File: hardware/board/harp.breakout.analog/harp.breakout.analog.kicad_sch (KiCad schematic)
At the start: 19 parts, among them J1 Conn_01x12_Socket, J10 Conn_01x01_Pin, J2 Conn_01x03_Pin, J3 Conn_01x03_Pin, J4 Conn_01x03_Pin, J5 Conn_02x10_Odd_Even, J6 Conn_01x03_Pin, J7 Conn_01x03_Pin, J8 Conn_01x03_Pin, J9 Conn_01x01_Pin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

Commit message: Analog Breakout layout
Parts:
- removed J10, J9: Conn_01x01_Pin, Connector_Pin:Pin_D1.0mm_L10.0mm, symbol Connector:Conn_01x01_Pin
- removed U5: TXB0108, Package_SO:TSSOP-20_4.4x6.5mm_P0.65mm, symbol Logic_LevelTranslator:TXB0108DQSR
- added J9: Conn_01x06_Pin, Connector_PinHeader_2.54mm:PinHeader_1x06_P2.54mm_Vertical, symbol Connector:Conn_01x06_Pin
- added U3: TXB0104D, Package_SO:SOIC-14_3.9x8.7mm_P1.27mm, symbol Logic_LevelTranslator:TXB0104D
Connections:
- net GNDA is gone; now on net GND: U1.14 (AGND)
- net IN2 is gone; now on net OUT0: J5.5 (Pin_5)
- net IN2_5V is gone; now on net OUT0_5V: J1.4 (Pin_4)
- net IN3 is gone; now on net OUT1: J5.7 (Pin_7)
- net IN3_5V is gone; now on net OUT1_5V: J1.1 (Pin_1)
- net +3.3V: now also J9.2 (Pin_2), U3.1 (VCCA)
- net +5V: now also J9.1 (Pin_1), U3.14 (VCCB)
- net A6: now also J9.3 (Pin_3)
- net A7: now also J9.4 (Pin_4)
- net GND: now also J9.5 (Pin_5), J9.6 (Pin_6), U3.7 (GND)
- net IN0: now also U3.2 (A1)
- net IN0_5V: now also U3.13 (B1)
- net IN1: now also U3.3 (A2)
- net IN1_5V: now also U3.12 (B2)
- net OUT0: now also U3.4 (A3)
- net OUT0_5V: now also U3.11 (B3)
- net OUT1: now also U3.5 (A4)
- net OUT1_5V: now also U3.10 (B4)
- net SPI_In: now also J5.11 (Pin_11); no longer J5.13 (Pin_13)
- net SPI_Out: now also J5.13 (Pin_13); no longer J5.11 (Pin_11)
- net at C5.1, R1.1: now also U3.8 (OE)
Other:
- note added: "Camera Triggers"
- note added: "Extra"
- note added: "Poke"
- moved on the sheet: C5, J1, J2, J3, J4, J6, J7, J8, R1

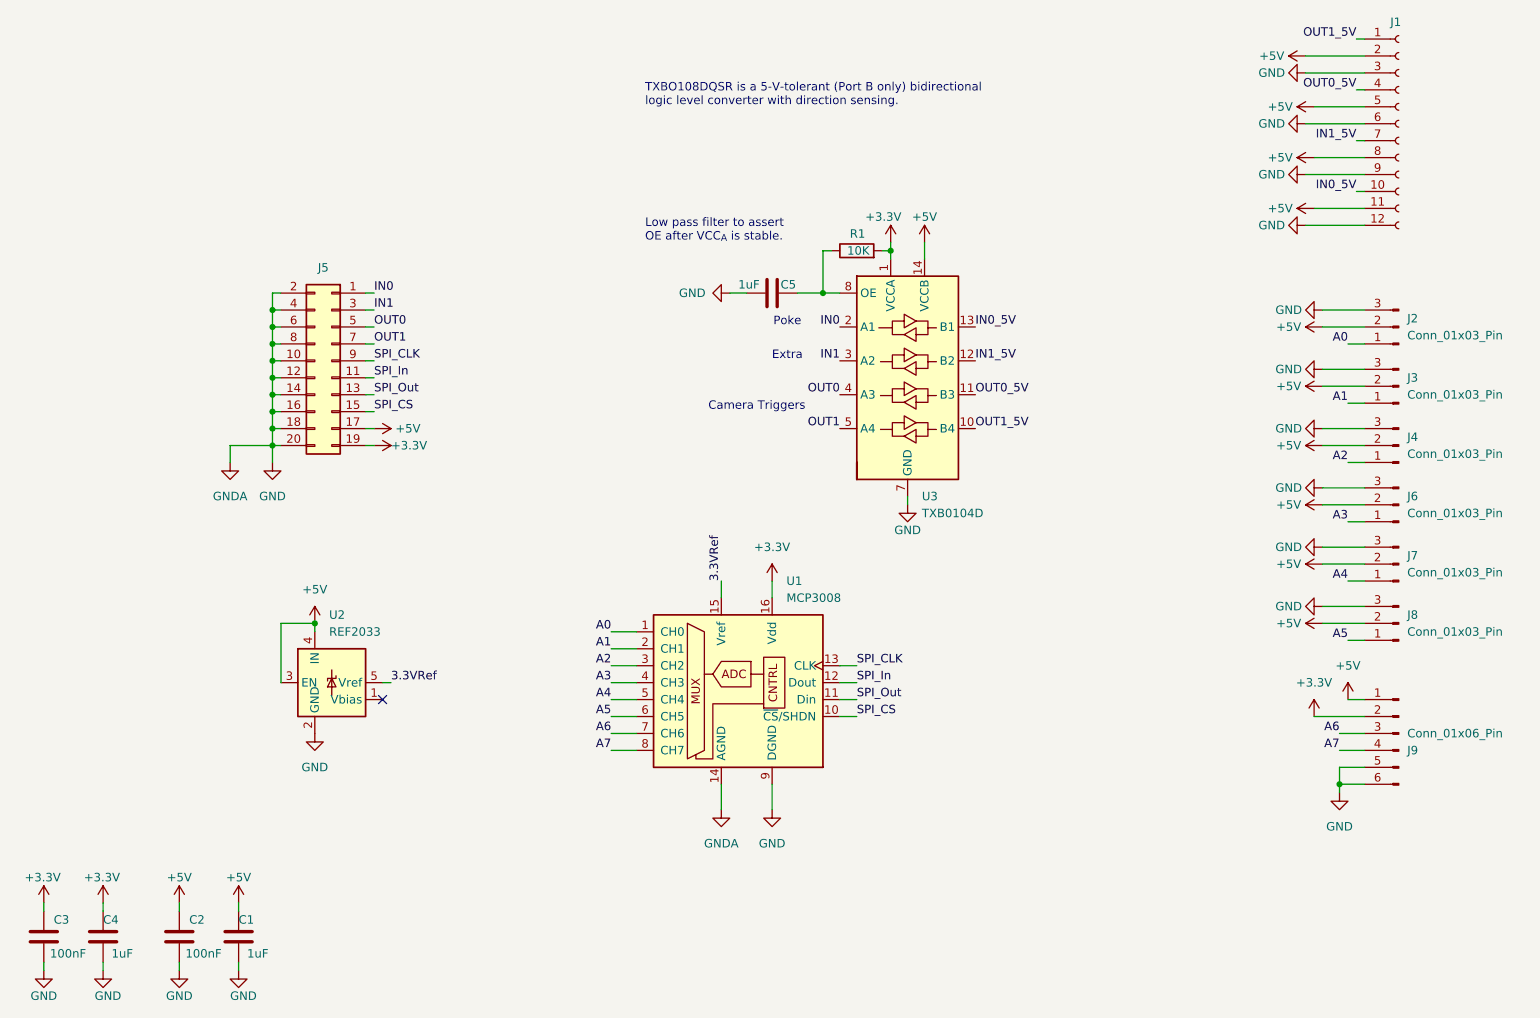
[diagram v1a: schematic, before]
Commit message: Added bypass caps and updated BOM
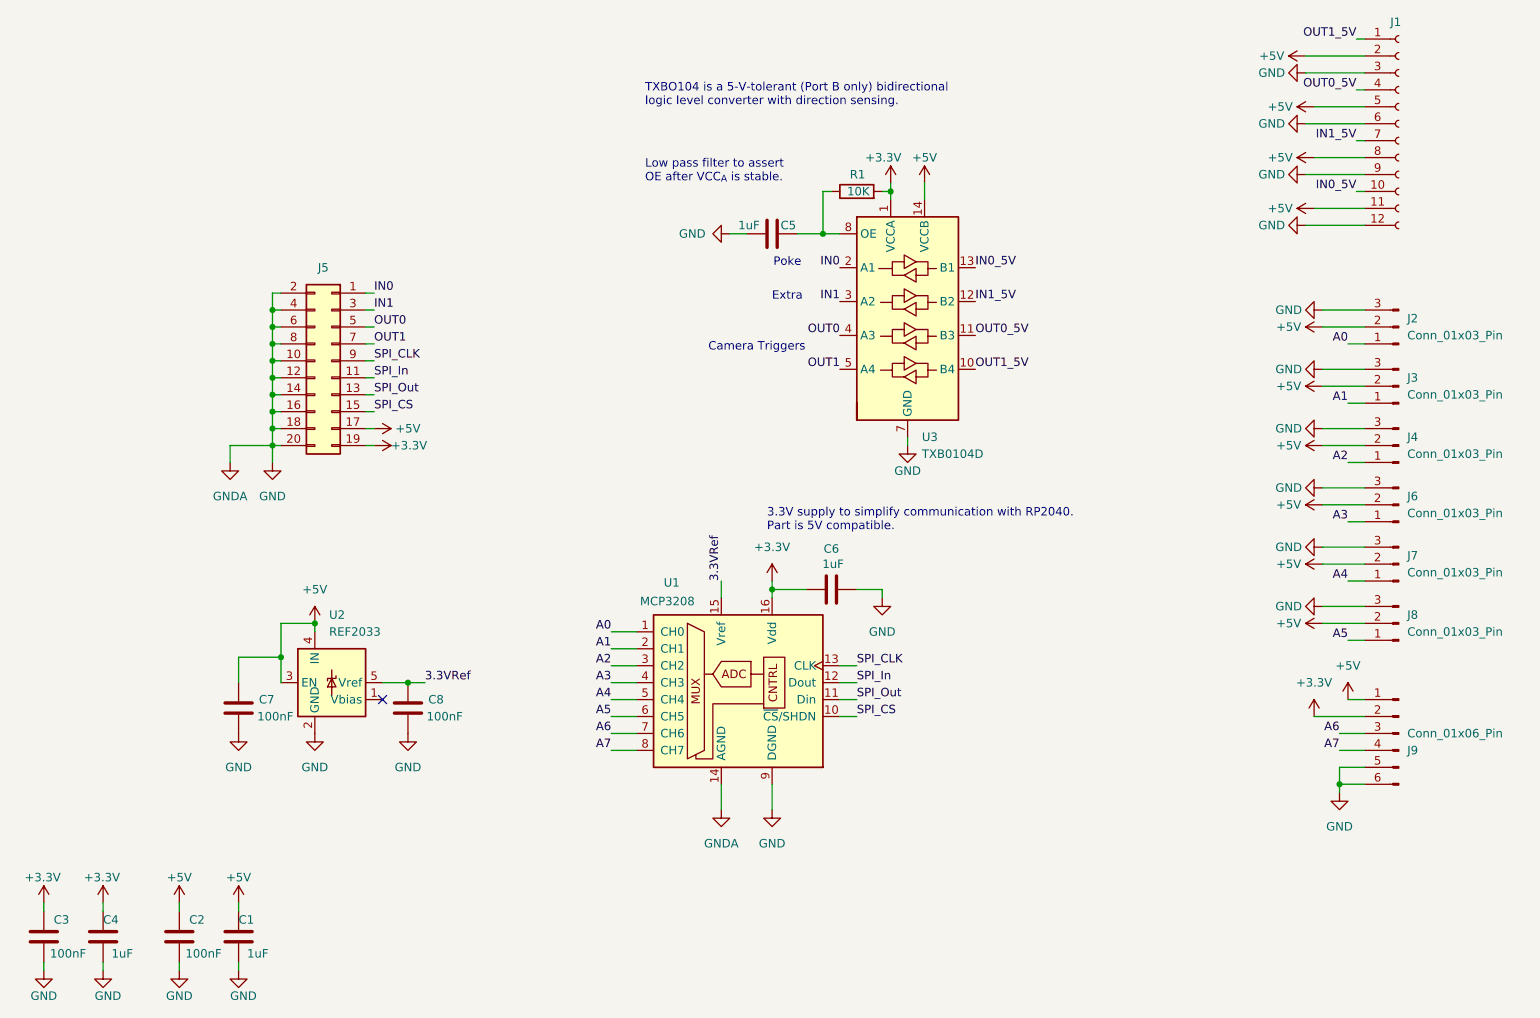
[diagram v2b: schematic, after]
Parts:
- added C6: 1uF, Capacitor_SMD:C_0402_1005Metric_Pad0.74x0.62mm_HandSolder, symbol Device:C
- added C7, C8: 100nF, Capacitor_SMD:C_0402_1005Metric_Pad0.74x0.62mm_HandSolder, symbol Device:C
- J2, J3, J4, J6, J7, J8: Link (none) -> https://www.digikey.com/en/products/detail/molex/0705530002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; Manufacturer (none) -> Molex; Manufacturer Number (none) -> 0705530002
- J9: Manufacturer (none) -> DNP; Manufacturer Number (none) -> DNP
- U1: value MCP3008 -> MCP3208; symbol Analog_ADC:MCP3008 -> Analog_ADC:MCP3208; Link (none) -> https://www.digikey.com/en/products/detail/microchip-techno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; Manufacturer (none) -> Microchip Technology; Manufacturer Number (none) -> MCP3208-CI/P
- U2: Link (none) -> https://www.digikey.com/en/products/detail/texas-instrument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; Manufacturer (none) -> TI; Manufacturer Number (none) -> REF2033QDDCRQ1
- U3: Link (none) -> https://www.digikey.com/en/products/detail/texas-instrument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; Manufacturer (none) -> TI; Manufacturer Number (none) -> TXB0104DR
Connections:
- net +3.3V: now also C6.1
- net +5V: now also C7.1
- net 3.3VRef: now also C8.1
- net GND: now also C6.2, C7.2, C8.2
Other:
- note added: "3.3V supply to simplify communication with RP2040. Part is 5V compatible."
- note added: "TXBO104 is a 5-V-tolerant (Port B only) bidirectional logic level converter with direction sensing."
- note removed: "TXBO108DQSR is a 5-V-tolerant (Port B only) bidirectional logic level converter with direction sensing."
- moved on the sheet: C5, R1, U3

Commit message: Improved silkscreen and corrected SPI pins
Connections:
- net SPI_In: now also U1.11 (Din); no longer U1.12 (Dout)
- net SPI_Out: now also U1.12 (Dout); no longer U1.11 (Din)
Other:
- note added: "Note: Din and Dout flipped from original prototype"
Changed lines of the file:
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@@
+		)
+	)
+	(text "Note: Din and Dout flipped \nfrom original prototype"
+		(exclude_from_sim no)
+		(at 173.228 138.43 0)
+		(effects
+			(font
+				(size 1.27 1.27)
+			)
 		)
 	)
@@
 	)
 	(label "SPI_In"
-		(at 149.86 138.43 0)
+		(at 149.86 140.97 0)
 		(effects
 			(font
@@
 	)
 	(label "SPI_Out"
-		(at 149.86 140.97 0)
-		(effects
-			(font
+		(at 149.86 138.43 0)
+		(effects
+			(font
